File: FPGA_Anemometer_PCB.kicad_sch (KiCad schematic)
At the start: 2 parts, among them J3 Conn_02x20_Top_Bottom, J4 Conn_02x20_Top_Bottom

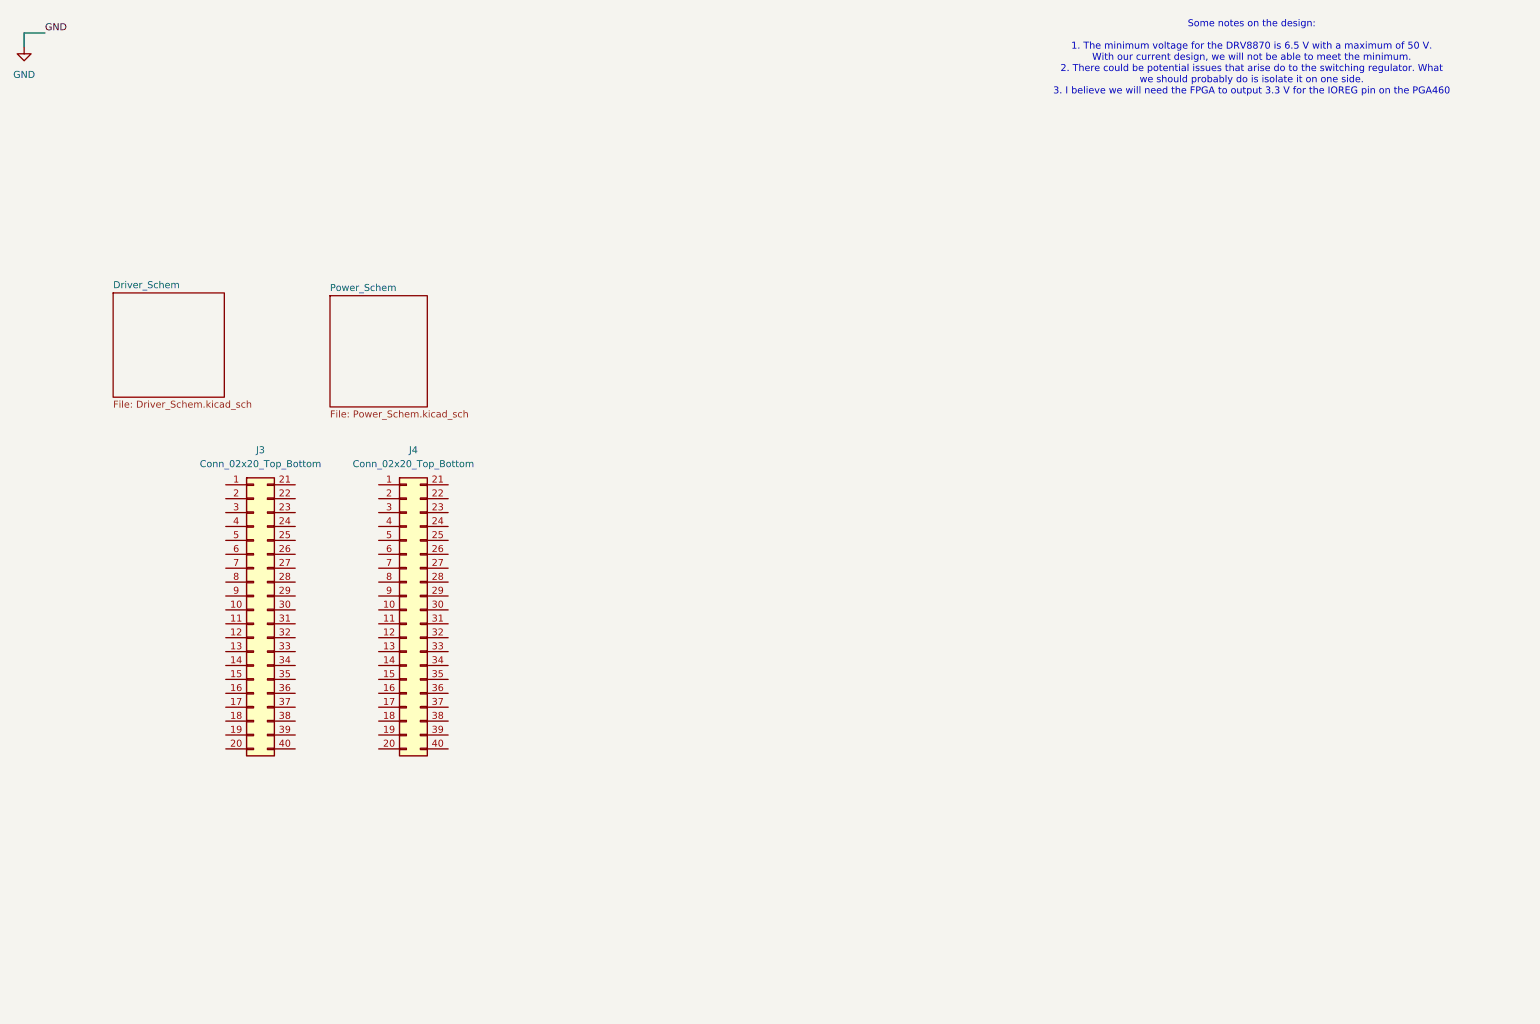
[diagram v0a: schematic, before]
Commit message: Add files via upload
New changes to the PCB
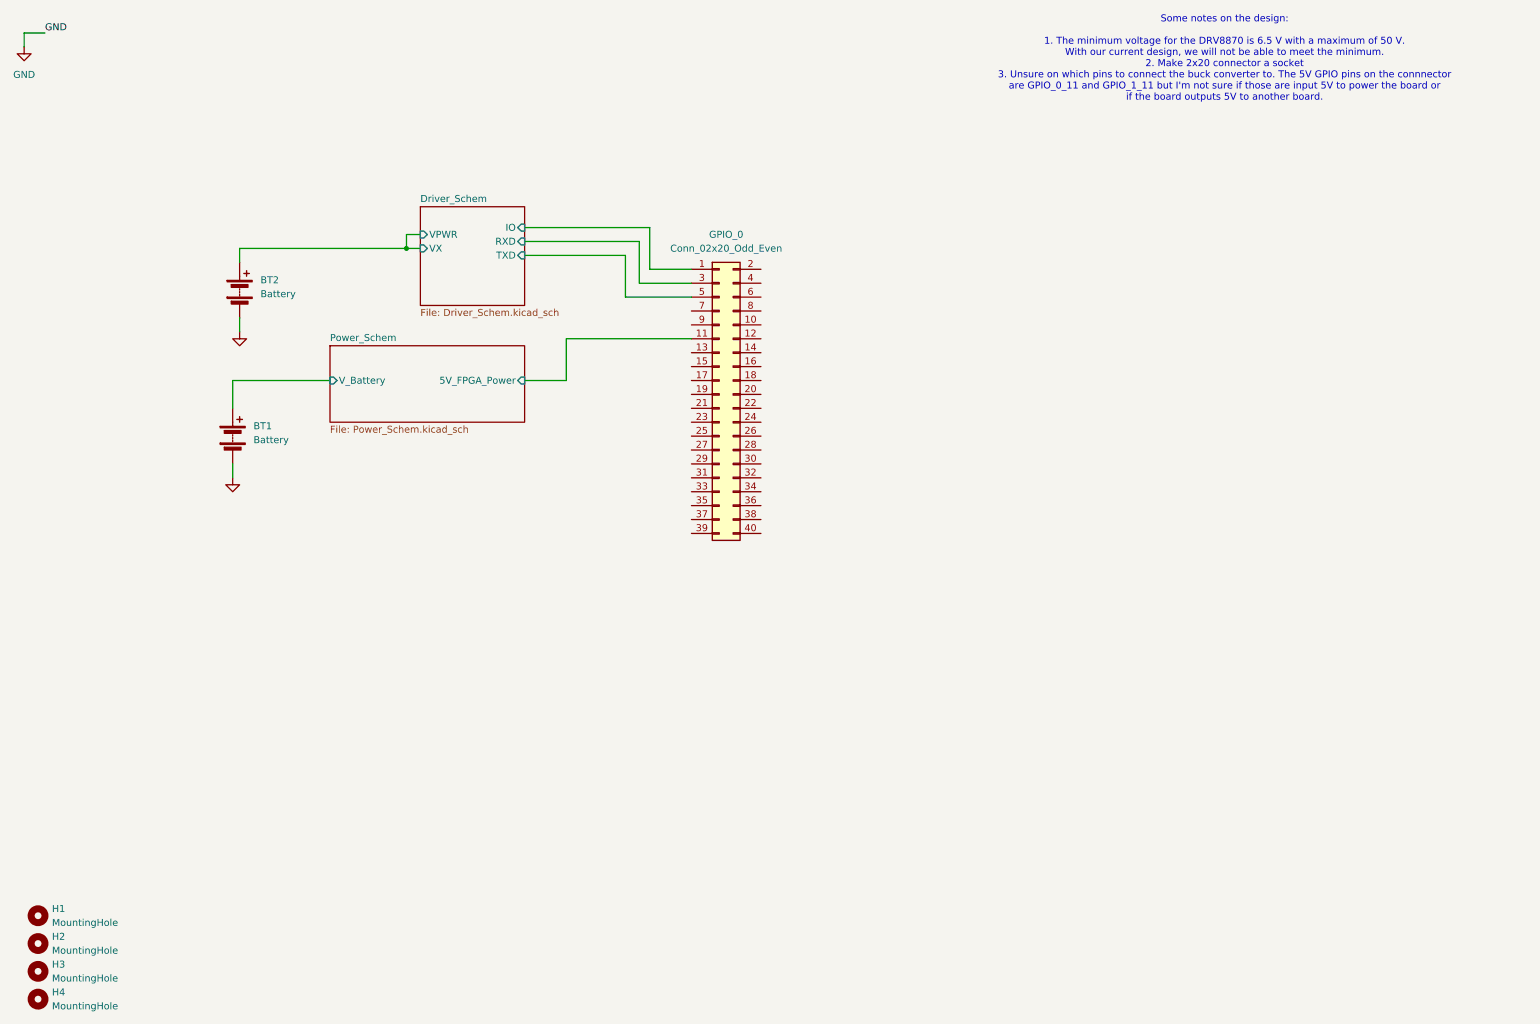
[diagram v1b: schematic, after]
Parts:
- removed J3, J4: Conn_02x20_Top_Bottom, symbol Connector_Generic:Conn_02x20_Top_Bottom
- added BT1, BT2: Battery, symbol Device:Battery
- added GPIO_0: Conn_02x20_Odd_Even, symbol Connector_Generic:Conn_02x20_Odd_Even
- added H1, H2, H3, H4: MountingHole, symbol Mechanical:MountingHole
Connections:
- net GND: now also BT1.2 (-), BT2.2 (-)
- new net Driver_Schem/IO: GPIO_0.1 (Pin_1)
- new net Driver_Schem/RXD: GPIO_0.3 (Pin_3)
- new net Driver_Schem/TXD: GPIO_0.5 (Pin_5)
- new net Driver_Schem/VPWR: BT2.1 (+)
- new net Power_Schem/5V_FPGA_Power: GPIO_0.11 (Pin_11)
- new net Power_Schem/V_Battery: BT1.1 (+)
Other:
- sheet Driver_Schem ports: added IO, RXD, TXD, VPWR, VX; removed none
- sheet Power_Schem ports: added 5V_FPGA_Power, V_Battery; removed none
- note added: "Some notes on the design: 1. The minimum voltage for the DRV8870 is 6.5 V with a maximum of 50 V. With our current design, we will not be able to meet the minimum. 2. Make 2x20 connector a socket 3. Unsure on which pins to connect the buck converter to. The 5V GPIO pins on the connnector are GPIO_0_11 and GPIO_1_11 but I'm not sure if those are input 5V to power the board or if the board outputs 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"
- note removed: "Some notes on the design: 1. The minimum voltage for the DRV8870 is 6.5 V with a maximum of 50 V. With our current design, we will not be able to meet the minimum. 2. There could be potential issues that arise do to the switching regulator. What we should probably do is isolate it on one side. 3. I believe we will need the FPGA to output 3.3 V for the IOREG pin on the PGA460"

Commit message: Add files via upload
This is the current PCB design. I am open to suggestions for changes.
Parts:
- removed BT1, BT2: Battery, symbol Device:Battery
- added J3, J4: YO0221500000G, YO0221500000G:CONN_YO0221500000G_AMP, symbol 2026-01-23_14-54-26:YO0221500000G
- GPIO_0: footprint (none) -> Connector_PinSocket_2.54mm:PinSocket_2x20_P2.54mm_Vertical
- H1, H2, H3, H4: footprint (none) -> MountingHole:MountingHole_3.2mm_M3
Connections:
- net Driver_Schem/VPWR: now also J3.1
- net GND: now also GPIO_0.12 (Pin_12), J3.2, J4.2
- net Power_Schem/V_Battery: now also J4.1

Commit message: Add files via upload
This will be the most up to date PCB. Throw the 3D viewer on and rotate it for an easter egg.
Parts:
- J3, J4: footprint YO0221500000G:CONN_YO0221500000G_AMP -> footprints:CONN_YO0221500000G_AMP
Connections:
- net GND: no longer GPIO_0.12 (Pin_12)
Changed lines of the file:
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@@
-	(wire
-		(pts
-			(xy 157.48 72.39) (xy 157.48 74.93)
-		)
-		(stroke
-			(width 0)
-			(type default)
-		)
-	)
 	(wire
 		(pts
@@
 		(pts
 			(xy 55.88 87.63) (xy 55.88 97.79)
-		)
-		(stroke
-			(width 0)
-			(type default)
-		)
-	)
-	(wire
-		(pts
-			(xy 152.4 72.39) (xy 157.48 72.39)
 		)
 		(stroke
@@
 			)
 		)
-		(property "Footprint" "YO0221500000G:CONN_YO0221500000G_AMP"
+		(property "Footprint" "footprints:CONN_YO0221500000G_AMP"
 			(at 57.15 60.96 0)
 			(effects
@@
 	)
 	(symbol
-		(lib_id "power:GND")
-		(at 157.48 74.93 0)
-		(unit 1)
-		(exclude_from_sim no)
-		(in_bom yes)
-		(on_board yes)
-		(dnp no)
-		(fields_autoplaced yes)
-		(property "Reference" "#PWR04"
-			(at 157.48 81.28 0)
-			(effects
-				(font
-					(size 1.27 1.27)
-				)
-				(hide yes)
-			)
-		)
-		(property "Value" "GND"
-			(at 157.48 80.01 0)
-			(effects
-				(font
-					(size 1.27 1.27)
-				)
-				(hide yes)
-			)
-		)
-		(property "Footprint" ""
-			(at 157.48 74.93 0)
-			(effects
-				(font
-					(size 1.27 1.27)
-				)
-				(hide yes)
-			)
-		)
-		(property "Datasheet" ""
-			(at 157.48 74.93 0)
-			(effects
-				(font
-					(size 1.27 1.27)
-				)
-				(hide yes)
-			)
-		)
-		(property "Description" "Power symbol creates a global label with name \"GND\" , ground"
-			(at 157.48 74.93 0)
-			(effects
-				(font
-					(size 1.27 1.27)
-				)
-				(hide yes)
-			)
-		)
-		(pin "1"
-		)
-		(instances
-			(project "FPGA_Anemometer_PCB"
-				(path "/f02116dc-3d6e-45e4-b4ab-5ea900e13651"
-					(reference "#PWR04")
-					(unit 1)
-				)
-			)
-		)
-	)
-	(symbol
 		(lib_id "2026-01-23_14-54-26:YO0221500000G")
 		(at 55.88 85.09 0)
@@
 			)
 		)
-		(property "Footprint" "YO0221500000G:CONN_YO0221500000G_AMP"
+		(property "Footprint" "footprints:CONN_YO0221500000G_AMP"
 			(at 55.88 85.09 0)
 			(effects
